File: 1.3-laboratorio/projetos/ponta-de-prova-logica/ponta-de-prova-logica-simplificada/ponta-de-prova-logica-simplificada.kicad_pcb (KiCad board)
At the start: 2 copper layers, 64.8 x 39.4 mm, 21 parts, among them J1 Conn_01x02, J2 PONTA DE PROVA, U1 LM339

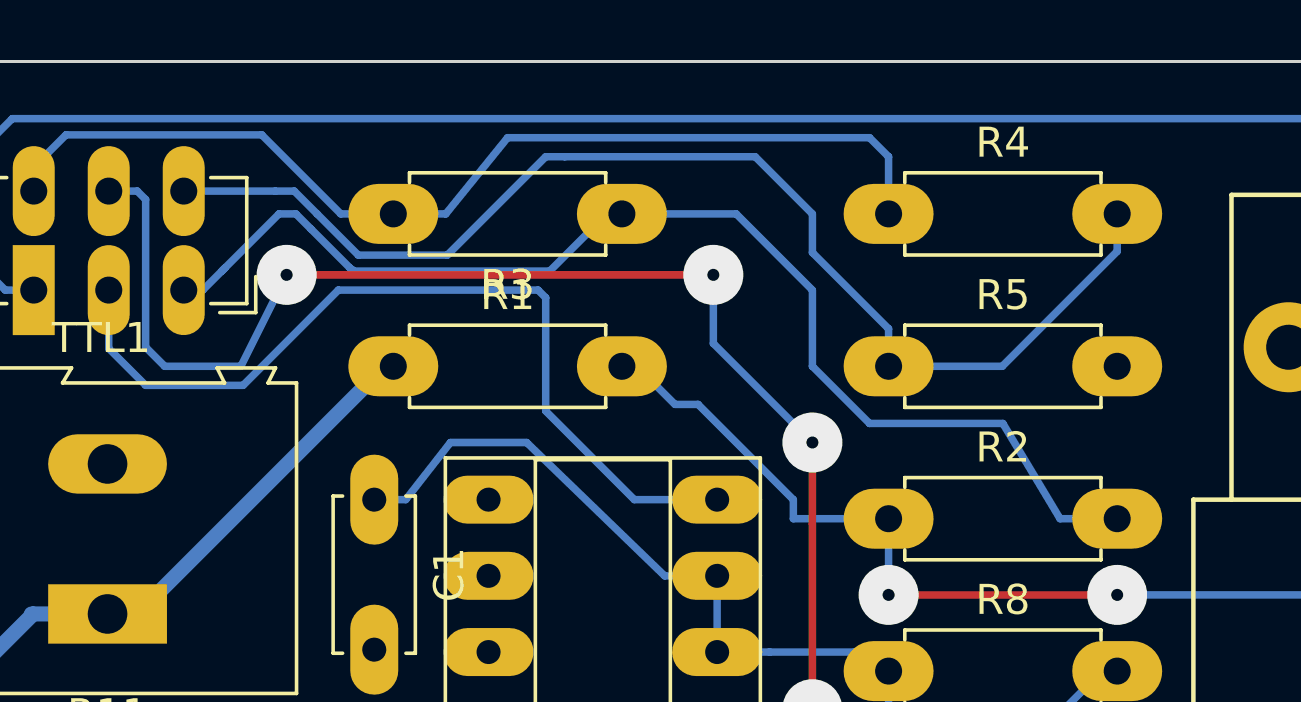
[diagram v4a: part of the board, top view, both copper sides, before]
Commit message: Versão final do roteamento da PCI da Ponta de Prova Lógica. Falta ajustes de F.SilkS. Adicionado no repositório, também, circuitos de simulação do LogiSim.
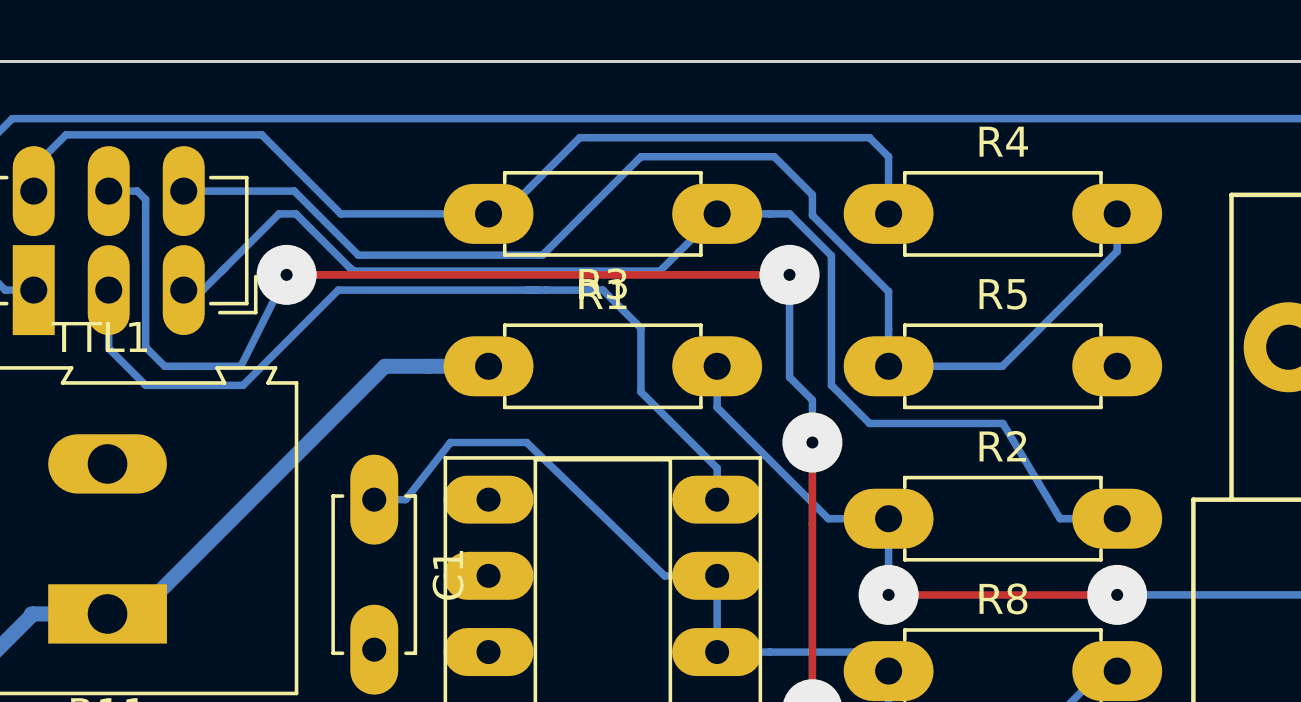
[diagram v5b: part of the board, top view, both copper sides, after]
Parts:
- moved R1 3.18 mm to (150.5, 91.4)
- moved R3 3.18 mm to (158.1, 86.4)
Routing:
- net Net-(R1-Pad2): track 103.5 -> 100.8 mm
- net VCC: track 100.1 -> 102.8 mm
- net Net-(R10-Pad1): track 62.9 -> 64.4 mm
- net Net-(R2-Pad2): track 40.7 -> 41.3 mm
